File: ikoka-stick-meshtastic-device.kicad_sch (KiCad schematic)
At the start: 26 parts, among them J1 Conn_Coaxial, J2 Conn_01x07_Socket, J3 Conn_01x07_Socket, J4 Conn_01x02, J5 Conn_01x02, J6 Conn_01x04, Q1 AO3401A, SW1 SW_Push, U1 MT3608, U2 E22-900M30S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

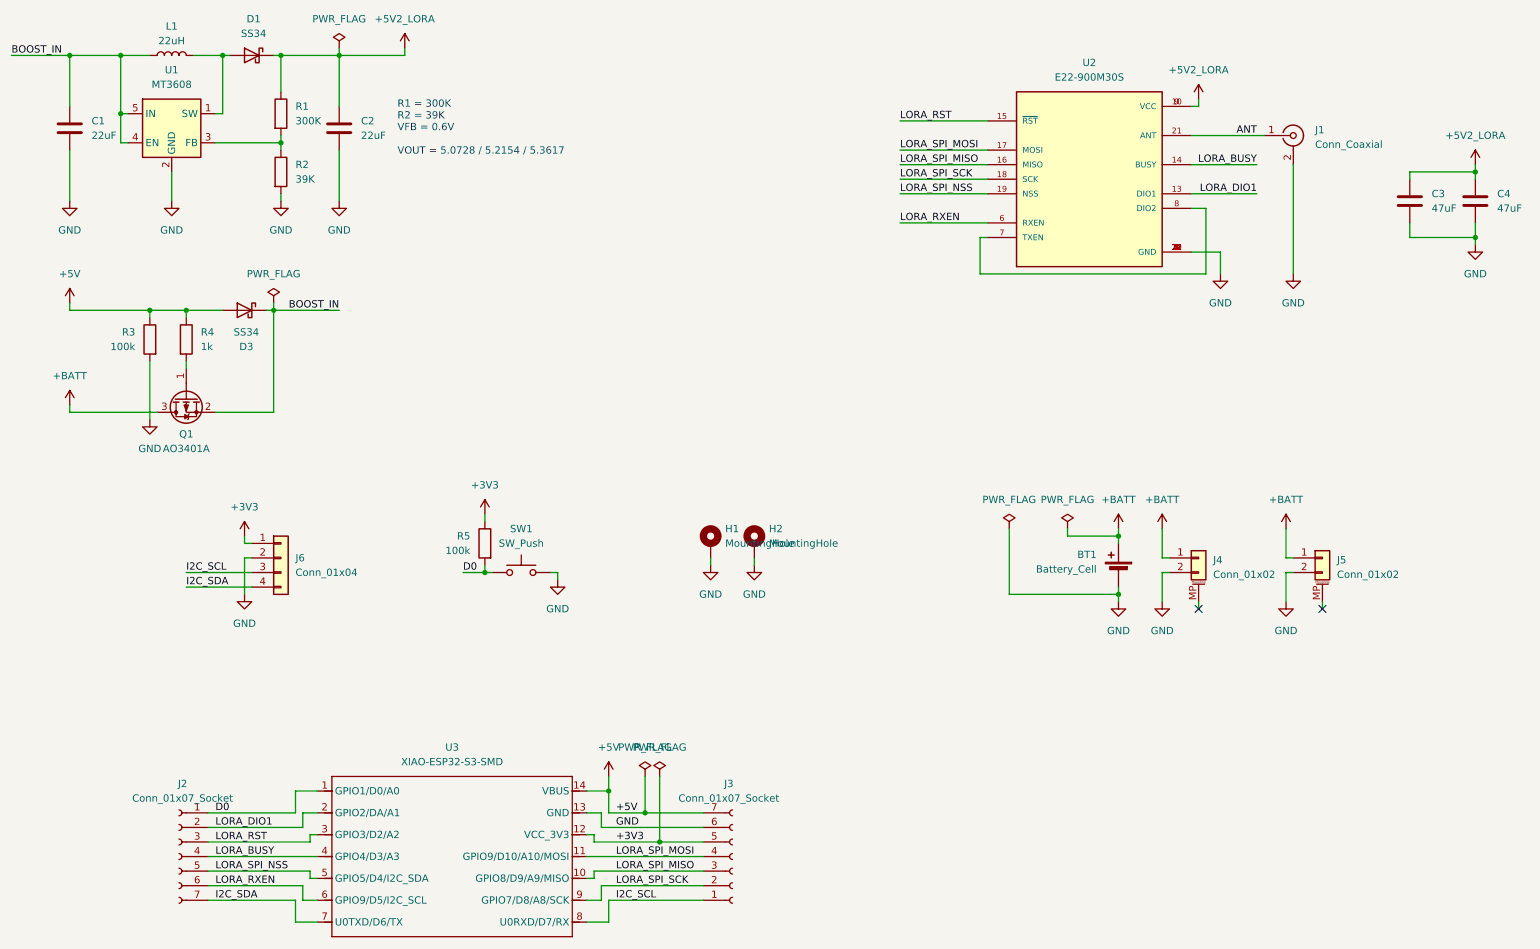
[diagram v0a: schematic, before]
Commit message: use E22P, swap I2C power/gnd
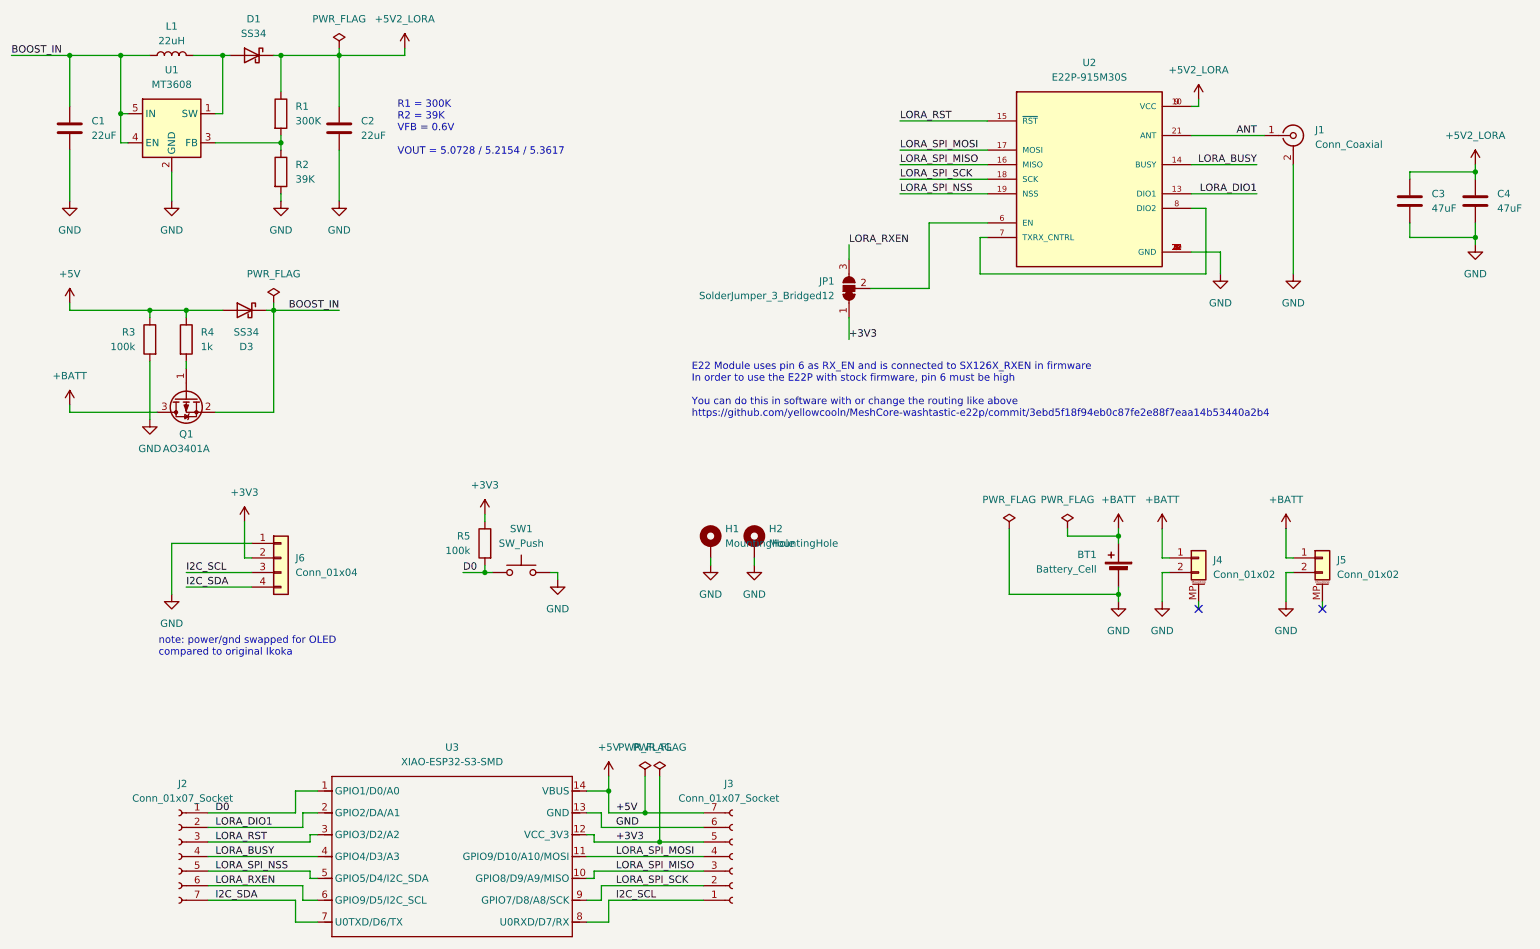
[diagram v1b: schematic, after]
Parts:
- added JP1: SolderJumper_3_Bridged12, Jumper:SolderJumper-3_P1.3mm_Bridged12_RoundedPad1.0x1.5mm_NumberLabels, symbol Jumper:SolderJumper_3_Bridged12
- U2: value E22-900M30S -> E22P-915M30S; symbol E22-900M30S:E22-900M30S -> _tahnok:E22P-915M30S
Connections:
- net +3V3: now also J6.2 (Pin_2), JP1.1 (A); no longer J6.1 (Pin_1)
- net GND: now also J6.1 (Pin_1); no longer J6.2 (Pin_2)
- net LORA_RXEN: now also JP1.3 (B); no longer U2.6 (RXEN)
- new net: JP1.2 (C), U2.6 (EN)
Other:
- note added: "E22 Module uses pin 6 as RX_EN and is connected to SX126X_RXEN in firmware In order to use the E22P with stock firmware, pin 6 must be high You can do this in software with or change the routing like above https://github.com/yellowcooln/MeshCore-washtastic-e22p/commit/3ebd5f18f94eb0c87fe2e88f7eaa14b53440a2b4"
- note added: "note: power/gnd swapped for OLED compared to original Ikoka"
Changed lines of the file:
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@@
 	(generator_version "9.0")
 	(paper "A4")
+	(text "note: power/gnd swapped for OLED\ncompared to original Ikoka"
+		(exclude_from_sim no)
+		(at 43.434 128.524 0)
+		(effects
+			(font
+				(size 1.27 1.27)
+			)
+			(justify left)
+		)
+	)
 	(text "R1 = 300K\nR2 = 39K\nVFB = 0.6V\n\nVOUT = 5.0728 / 5.2154 / 5.3617"
 		(exclude_from_sim no)
@@
 		)
 	)
+	(text "E22 Module uses pin 6 as RX_EN and is connected to SX126X_RXEN in firmware\nIn order to use the E22P with stock firmware, pin 6 must be high\n\nYou can do this in software with or change the routing like above\nhttps://github.com/yellowcooln/MeshCore-washtastic-e22p/commit/3ebd5f18f94eb0c87fe2e88f7eaa14b53440a2b4"
+		(exclude_from_sim no)
+		(at 136.398 83.82 0)
+		(effects
+			(font
+				(size 1.27 1.27)
+			)
+			(justify left)
+		)
+	)
 	(junction
 		(at 100.33 115.57)
@@
 	(wire
 		(pts
-			(xy 59.69 113.03) (xy 58.42 113.03)
-		)
-		(stroke
-			(width 0)
-			(type default)
-		)
-	)
-	(wire
-		(pts
 			(xy 54.61 25.4) (xy 54.61 35.56)
 		)
@@
 	(wire
 		(pts
-			(xy 210.82 109.22) (xy 210.82 110.49)
+			(xy 167.64 66.04) (xy 177.8 66.04)
 		)
 		(stroke
@@
 	(wire
 		(pts
-			(xy 210.82 120.65) (xy 210.82 119.38)
+			(xy 210.82 109.22) (xy 210.82 110.49)
 		)
 		(stroke
@@
 	(wire
 		(pts
-			(xy 69.85 168.91) (xy 71.12 168.91)
+			(xy 210.82 120.65) (xy 210.82 119.38)
 		)
 		(stroke
@@
 	(wire
 		(pts
-			(xy 172.72 54.61) (xy 187.96 54.61)
+			(xy 69.85 168.91) (xy 71.12 168.91)
 		)
 		(stroke
@@
 	(wire
 		(pts
-			(xy 58.42 109.22) (xy 58.42 110.49)
-		)
-		(stroke
-			(width 0)
-			(type default)
-		)
-	)
-	(wire
-		(pts
 			(xy 36.83 40.64) (xy 38.1 40.64)
 		)
@@
 	(wire
 		(pts
-			(xy 58.42 113.03) (xy 58.42 119.38)
-		)
-		(stroke
-			(width 0)
-			(type default)
-		)
-	)
-	(wire
-		(pts
 			(xy 63.5 69.85) (xy 74.93 69.85)
 		)
@@
 	(wire
 		(pts
+			(xy 59.69 110.49) (xy 45.72 110.49)
+		)
+		(stroke
+			(width 0)
+			(type default)
+		)
+	)
+	(wire
+		(pts
 			(xy 223.52 59.69) (xy 228.6 59.69)
 		)
@@
 	(wire
 		(pts
+			(xy 177.8 66.04) (xy 177.8 54.61)
+		)
+		(stroke
+			(width 0)
+			(type default)
+		)
+	)
+	(wire
+		(pts
 			(xy 224.79 33.02) (xy 224.79 34.29)
 		)
@@
 	(wire
 		(pts
-			(xy 111.76 115.57) (xy 113.03 115.57)
+			(xy 58.42 106.68) (xy 58.42 113.03)
 		)
 		(stroke
@@
 	(wire
 		(pts
-			(xy 27.94 86.36) (xy 27.94 87.63)
+			(xy 111.76 115.57) (xy 113.03 115.57)
 		)
 		(stroke
@@
 	(wire
 		(pts
-			(xy 59.69 110.49) (xy 58.42 110.49)
+			(xy 27.94 86.36) (xy 27.94 87.63)
 		)
 		(stroke
@@
 	(wire
 		(pts
+			(xy 177.8 54.61) (xy 187.96 54.61)
+		)
+		(stroke
+			(width 0)
+			(type default)
+		)
+	)
+	(wire
+		(pts
 			(xy 261.62 45.72) (xy 261.62 46.99)
 		)
@@
 	(wire
 		(pts
+			(xy 163.83 58.42) (xy 163.83 60.96)
+		)
+		(stroke
+			(width 0)
+			(type default)
+		)
+	)
+	(wire
+		(pts
 			(xy 74.93 25.4) (xy 74.93 34.29)
 		)
@@
 	(wire
 		(pts
+			(xy 59.69 113.03) (xy 58.42 113.03)
+		)
+		(stroke
+			(width 0)
+			(type default)
+		)
+	)
+	(wire
+		(pts
 			(xy 223.52 49.53) (xy 234.95 49.53)
 		)
@@
 	(wire
 		(pts
+			(xy 45.72 110.49) (xy 45.72 119.38)
+		)
+		(stroke
+			(width 0)
+			(type default)
+		)
+	)
+	(wire
+		(pts
 			(xy 54.61 35.56) (xy 53.34 35.56)
 		)
@@
 	(wire
 		(pts
+			(xy 163.83 71.12) (xy 163.83 74.93)
+		)
+		(stroke
+			(width 0)
+			(type default)
+		)
+	)
+	(wire
+		(pts
 			(xy 120.65 170.18) (xy 138.43 170.18)
 		)
@@
 	)
 	(label "LORA_RXEN"
-		(at 172.72 54.61 0)
+		(at 163.83 58.42 0)
 		(effects
 			(font
@@
 		)
 	)
+	(label "+3V3"
+		(at 163.83 74.93 0)
+		(effects
+			(font
+				(size 1.27 1.27)
+			)
+			(justify left bottom)
+		)
+	)
 	(label "D0"
 		(at 53.34 157.48 0)
@@
 	)
 	(symbol
-		(lib_id "E22-900M30S:E22-900M30S")
+		(lib_id "_tahnok:E22P-915M30S")
 		(at 205.74 46.99 0)
 		(unit 1)
@@
 			)
 		)
-		(property "Value" "E22-900M30S"
+		(property "Value" "E22P-915M30S"
 			(at 205.74 29.21 0)
 			(effects
@@
 			)
 		)
-		(property "Datasheet" ""
+		(property "Datasheet" "https://cdn.tahnok.ca/u/E22P-xxxMxxS_UserManual_ES_v1.0.pdf"
 			(at 205.74 46.99 0)
 			(effects
@@
 	(symbol
 		(lib_id "power:GND")
-		(at 58.42 119.38 0)
+		(at 45.72 119.38 0)
 		(unit 1)
 		(exclude_from_sim no)
@@
 		(fields_autoplaced yes)
 		(property "Reference" "#PWR015"
-			(at 58.42 125.73 0)
+			(at 45.72 125.73 0)
 			(effects
 				(font
@@
 		)
 		(property "Value" "GND"
-			(at 58.42 124.46 0)
+			(at 45.72 124.46 0)
 			(effects
 				(font
@@
 		)
 		(property "Footprint" ""
-			(at 58.42 119.38 0)
+			(at 45.72 119.38 0)
 			(effects
 				(font
@@
 		)
 		(property "Datasheet" ""
-			(at 58.42 119.38 0)
+			(at 45.72 119.38 0)
 			(effects
 				(font
@@
 		)
 		(property "Description" "Power symbol creates a global label with name \"GND\" , ground"
-			(at 58.42 119.38 0)
+			(at 45.72 119.38 0)
 			(effects
 				(font
@@
 	(symbol
 		(lib_id "power:+3V3")
-		(at 58.42 109.22 0)
+		(at 58.42 106.68 0)
 		(unit 1)
 		(exclude_from_sim no)
@@
 		(fields_autoplaced yes)
 		(property "Reference" "#PWR014"
-			(at 58.42 113.03 0)
+			(at 58.42 110.49 0)
 			(effects
 				(font
@@
 		)
 		(property "Value" "+3V3"
-			(at 58.42 104.14 0)
+			(at 58.42 101.6 0)
 			(effects
 				(font
@@
 		)
 		(property "Footprint" ""
-			(at 58.42 109.22 0)
+			(at 58.42 106.68 0)
 			(effects
 				(font
@@
 		)
 		(property "Datasheet" ""
-			(at 58.42 109.22 0)
+			(at 58.42 106.68 0)
 			(effects
 				(font
@@
 		)
 		(property "Description" "Power symbol creates a global label with name \"+3V3\""
-			(at 58.42 109.22 0)
+			(at 58.42 106.68 0)
 			(effects
 				(font
@@
 					(unit 1)
 				)
+			)
+		)
+	)
+	(symbol
+		(lib_id "Jumper:SolderJumper_3_Bridged12")
+		(at 163.83 66.04 90)
+		(unit 1)
+		(exclude_from_sim no)
+		(in_bom no)
+		(on_board yes)
+		(dnp no)
+		(fields_autoplaced yes)
+		(property "Reference" "JP1"
+			(at 161.29 64.7699 90)
+			(effects
+				(font
+					(size 1.27 1.27)
+				)
+				(justify left)
+			)
+		)
+		(property "Value" "SolderJumper_3_Bridged12"
+			(at 161.29 67.3099 90)
+			(effects
+				(font
+					(size 1.27 1.27)
+				)
+				(justify left)
+			)
+		)
+		(property "Footprint" "Jumper:SolderJumper-3_P1.3mm_Bridged12_RoundedPad1.0x1.5mm_NumberLabels"
+			(at 163.83 66.04 0)
+			(effects
+				(font
+					(size 1.27 1.27)
+				)
+				(hide yes)
+			)
+		)
+		(property "Datasheet" "~"
+			(at 163.83 66.04 0)
+			(effects
+				(font
+					(size 1.27 1.27)
+				)
+				(hide yes)
+			)
+		)
+		(property "Description" "3-pole Solder Jumper, pins 1+2 closed/bridged"
+			(at 163.83 66.04 0)
+			(effects
+				(font
+					(size 1.27 1.27)
+				)
+				(hide yes)
+			)
+		)
+		(pin "3"
+		)
+		(pin "2"
+		)
+		(pin "1"
+		)
+		(instances
+			(project ""
+				(path "/d817f34c-2aa5-4c70-878b-29719eb987fe"
+					(reference "JP1")
+					(unit 1)
+				)
